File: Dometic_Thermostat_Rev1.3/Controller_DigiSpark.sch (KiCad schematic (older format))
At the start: 22 parts, among them P1 UNREG_12V_IN, P2 UNUSED_MICRO_PINS, P3 RELAY_SW_OUT, P4 RELAY_NC, P5 FUSE_BLOCK, P6 AUX_VOLT_CONN, Q1 2N3904, Q2 2N2222A, T1 Relay_SPDT, U1 7805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

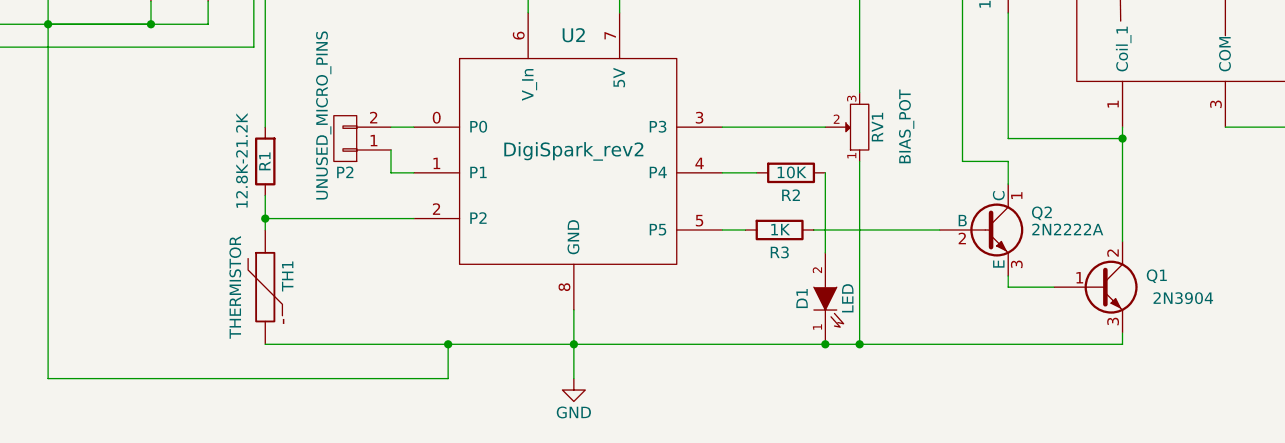
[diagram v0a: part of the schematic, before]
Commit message: Added R4 in || w/ thermistor, value not calculated
Changed thermistor config to series-parallel, increase linearity.
Method detailed at:

http://www.edn.com/design/sensors/4429105/Linearize-thermistors-with-new-formula
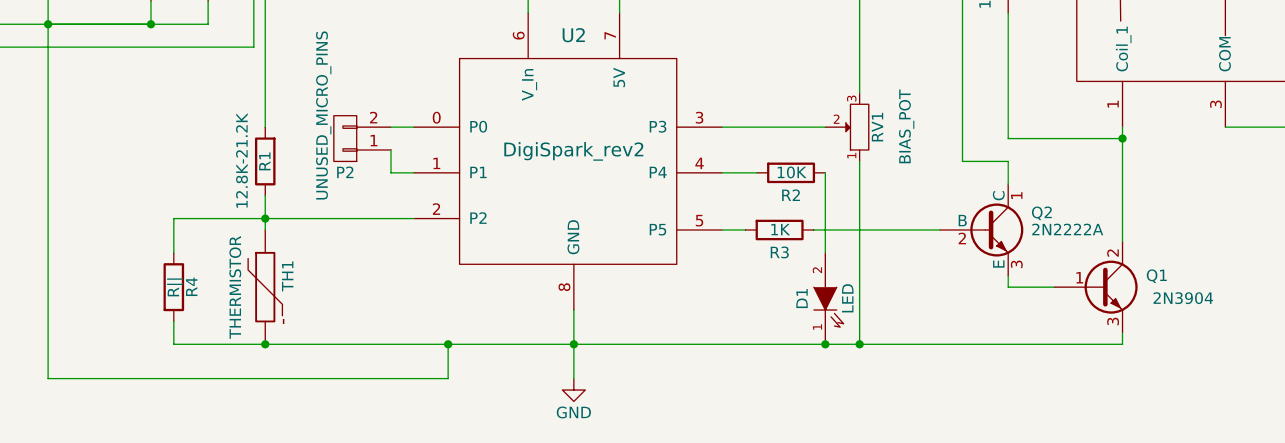
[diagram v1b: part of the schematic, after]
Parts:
- added R4: R||, Resistors_ThroughHole:R_Axial_DIN0309_L9.0mm_D3.2mm_P12.70mm_Horizontal, symbol R
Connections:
- net GND: now also R4.2
- net at R1.1, TH1.1, U2.2 (P2): now also R4.1
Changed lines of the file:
@@
 	2550 3000 2550 3150
 Wire Wire Line
-	3200 3100 2550 3100
+	2150 3100 3200 3100
 Connection ~ 2550 3100
 Wire Wire Line
-	2550 3650 6300 3650
+	2150 3650 6300 3650
 Connection ~ 3900 3650
 Wire Wire Line
@@
 Wire Wire Line
 	6300 3650 6300 3600
+$Comp
+L R R4
+U 1 1 59015000
+P 2150 3400
+F 0 "R4" V 2230 3400 50  0000 C CNN
+F 1 "R||" V 2150 3400 50  0000 C CNN
+F 2 "Resistors_ThroughHole:R_Axial_DIN0309_L9.0mm_D3.2mm_P12.70mm_Horizontal" V 2080 3400 50  0001 C CNN
+F 3 "" H 2150 3400 50  0000 C CNN
+	1    2150 3400
+	1    0    0    -1
+$EndComp
+Wire Wire Line
+	2150 3250 2150 3100
+Wire Wire Line
+	2150 3550 2150 3650
+Connection ~ 2550 3650
 $EndSCHEMATC

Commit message: Add R4, change footprints TH1 & LED
Added R4 to board, changed thermistor and LED footprints.
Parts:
- D1: footprint LEDs:LED_D3.0mm -> LEDs:LED_D5.0mm
- TH1: footprint COMPLIB:SolderWirePad_2x_1-5mmDrill-CUSTOMWIDE -> COMPLIB:Therm_Wire_Mounts
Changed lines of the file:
@@
 F 0 "TH1" V 2650 3450 50  0000 C CNN
 F 1 "THERMISTOR" V 2450 3400 50  0000 C BNN
-F 2 "COMPLIB:SolderWirePad_2x_1-5mmDrill-CUSTOMWIDE" H 2550 3400 50  0001 C CNN
+F 2 "COMPLIB:Therm_Wire_Mounts" H 2550 3400 50  0001 C CNN
 F 3 "" H 2550 3400 50  0000 C CNN
 	1    2550 3400
@@
 F 0 "D1" H 5000 3550 50  0000 C CNN
 F 1 "LED" H 5000 3350 50  0000 C CNN
-F 2 "LEDs:LED_D3.0mm" H 5000 3450 50  0001 C CNN
+F 2 "LEDs:LED_D5.0mm" H 5000 3450 50  0001 C CNN
 F 3 "" H 5000 3450 50  0000 C CNN
 	1    5000 3450

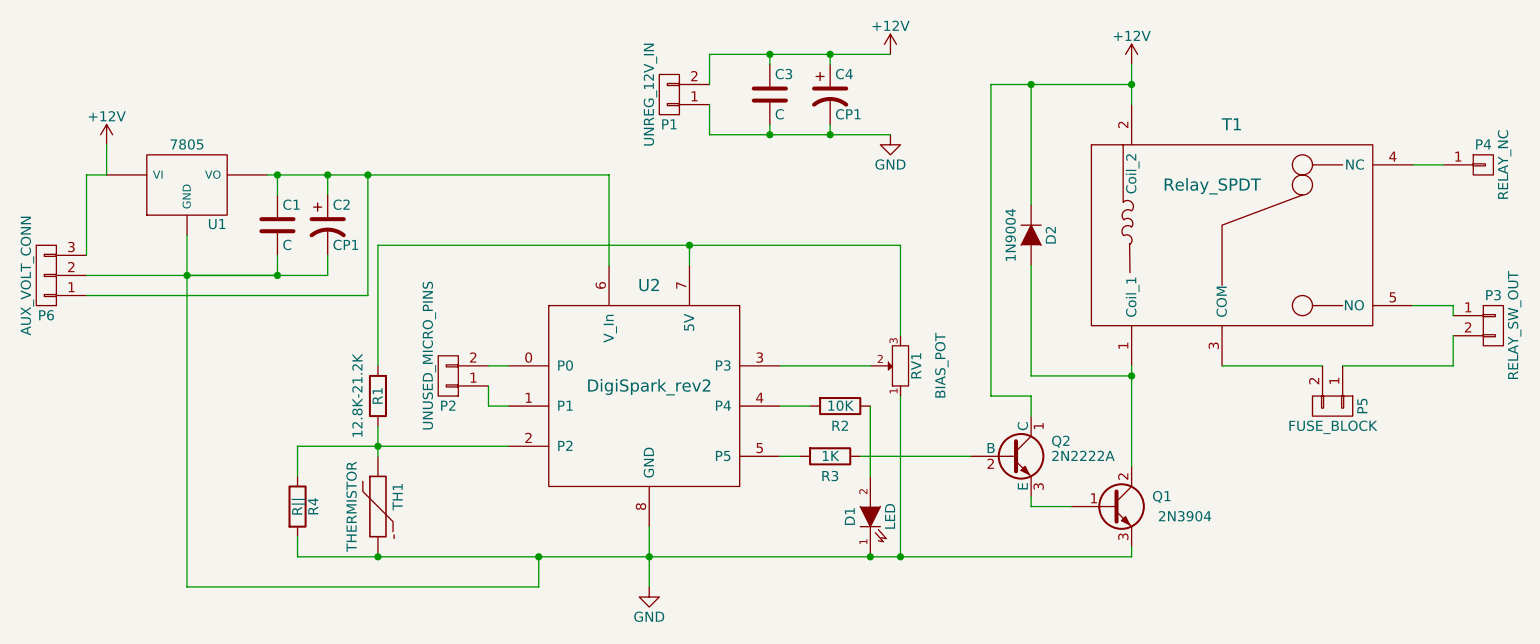
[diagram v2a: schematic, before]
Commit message: Changed Schematic-updated relay driver to mosfet
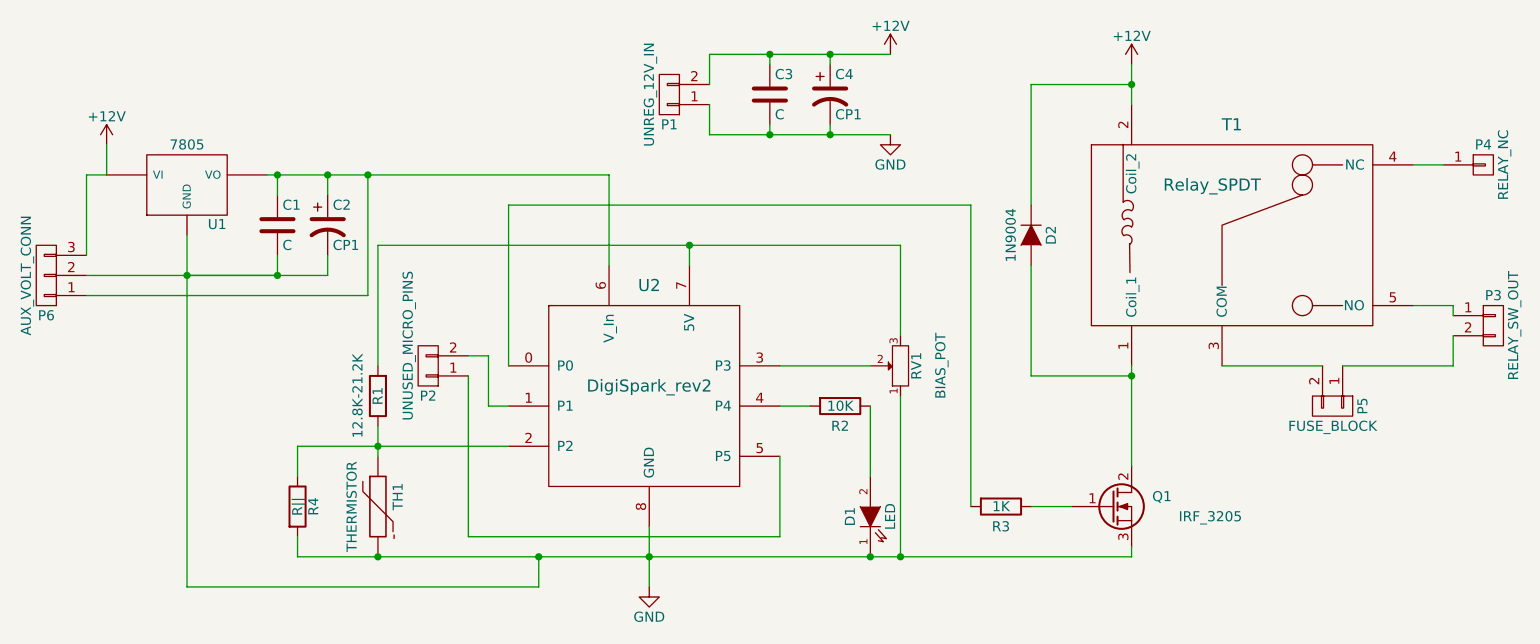
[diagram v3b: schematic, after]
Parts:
- removed Q1: 2N3904, TO_SOT_Packages_THT:TO-220_Horizontal, symbol Q_NPN_BCE
- removed Q2: 2N2222A, TO_SOT_Packages_THT:TO-92_Inline_Wide, symbol BC413
- added Q1: IRF_3205, symbol Q_NMOS_GDS
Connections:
- net GND: now also Q1.3 (S)
- net at U2.0 (P0): now also R3.2; no longer P2.2 (P2)
- net at U2.1 (P1): now also P2.2 (P2); no longer P2.1 (P1)
- net at U2.5 (P5): now also P2.1 (P1); no longer R3.2
- net at R3.1: now also Q1.1 (G)
- net at D2.2 (A), T1.1 (Coil_1): now also Q1.2 (D)
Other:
- moved on the sheet: P2, R3
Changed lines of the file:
@@
 L R R3
 U 1 1 58FFC6C2
-P 4800 3150
-F 0 "R3" V 4900 3150 50  0000 C CNN
-F 1 "1K" V 4800 3150 50  0000 C CNN
-F 2 "Resistors_ThroughHole:R_Axial_DIN0309_L9.0mm_D3.2mm_P12.70mm_Horizontal" V 4730 3150 50  0001 C CNN
-F 3 "" H 4800 3150 50  0000 C CNN
-	1    4800 3150
+P 5650 3400
+F 0 "R3" V 5750 3400 50  0000 C CNN
+F 1 "1K" V 5650 3400 50  0000 C CNN
+F 2 "Resistors_ThroughHole:R_Axial_DIN0309_L9.0mm_D3.2mm_P12.70mm_Horizontal" V 5580 3400 50  0001 C CNN
+F 3 "" H 5650 3400 50  0000 C CNN
+	1    5650 3400
 	0    1    1    0
-$EndComp
-$Comp
-L Q_NPN_BCE Q1
-U 1 1 58FFC83C
-P 6200 3400
-F 0 "Q1" H 6500 3450 50  0000 R CNN
-F 1 "2N3904" H 6700 3350 50  0000 R CNN
-F 2 "TO_SOT_Packages_THT:TO-220_Horizontal" H 6400 3500 50  0001 C CNN
-F 3 "" H 6200 3400 50  0000 C CNN
-	1    6200 3400
-	1    0    0    -1
 $EndComp
 $Comp
@@
 L CONN_01X02 P2
 U 1 1 58FFEBFE
-P 2900 2750
-F 0 "P2" H 2900 2900 50  0000 C CNN
-F 1 "UNUSED_MICRO_PINS" V 3000 2650 50  0000 C CNN
-F 2 "Pin_Headers:Pin_Header_Straight_1x02_Pitch2.00mm" H 2900 2750 50  0001 C CNN
-F 3 "" H 2900 2750 50  0000 C CNN
-	1    2900 2750
+P 2800 2700
+F 0 "P2" H 2800 2850 50  0000 C CNN
+F 1 "UNUSED_MICRO_PINS" V 2900 2600 50  0000 C CNN
+F 2 "Pin_Headers:Pin_Header_Straight_1x02_Pitch2.00mm" H 2800 2700 50  0001 C CNN
+F 3 "" H 2800 2700 50  0000 C CNN
+	1    2800 2700
 	-1   0    0    1
 $EndComp
@@
 	1    0    0    -1
 $EndComp
-Wire Wire Line
-	5000 2700 4550 2700
-Wire Wire Line
-	5150 2100 5150 2550
-Wire Wire Line
-	4550 2900 4700 2900
-Wire Wire Line
-	3900 3500 3900 3800
-Wire Wire Line
-	2550 3000 2550 3150
-Wire Wire Line
-	2150 3100 3200 3100
-Connection ~ 2550 3100
-Wire Wire Line
-	2150 3650 6300 3650
-Connection ~ 3900 3650
-Wire Wire Line
-	2550 2700 2550 2100
-Wire Wire Line
-	2550 2100 5150 2100
-Wire Wire Line
-	4100 2100 4100 2200
-Wire Wire Line
-	2000 1750 3700 1750
-Wire Wire Line
-	3700 1750 3700 2200
-Wire Wire Line
-	1600 3800 3350 3800
-Wire Wire Line
-	3350 3800 3350 3650
-Connection ~ 3350 3650
-Connection ~ 4100 2100
-Wire Wire Line
-	5000 2900 5000 3250
-Wire Wire Line
-	5150 3650 5150 2850
-Connection ~ 5000 3650
-Connection ~ 5150 3650
-Wire Wire Line
-	6300 2700 6300 3200
-Wire Wire Line
-	6300 1200 6300 1400
-Wire Wire Line
-	5800 1900 5800 1300
-Wire Wire Line
-	5600 1300 6300 1300
-Connection ~ 6300 1300
-Wire Wire Line
-	3100 2700 3200 2700
-Wire Wire Line
-	3100 2800 3100 2900
-Wire Wire Line
-	3100 2900 3200 2900
-Wire Wire Line
-	4200 1550 5100 1550
-Wire Wire Line
-	4800 1550 4800 1500
-Wire Wire Line
-	4500 1550 4500 1500
-Connection ~ 4800 1550
-Wire Wire Line
-	4200 1550 4200 1400
-Connection ~ 4500 1550
-Wire Wire Line
-	4200 1300 4200 1150
-Wire Wire Line
-	4200 1150 5100 1150
-Wire Wire Line
-	4500 1150 4500 1200
-Wire Wire Line
-	4800 1150 4800 1200
-Connection ~ 4500 1150
-Connection ~ 4800 1150
-Wire Wire Line
-	2300 1750 2300 1850
-Connection ~ 2300 1750
-Wire Wire Line
-	2050 1750 2050 1850
-Connection ~ 2050 1750
-Wire Wire Line
-	1200 1600 1200 1750
 $Comp
 L Relay_SPDT T1
@@
 	1    0    0    -1
 $EndComp
-Wire Wire Line
-	7700 2400 7900 2400
-Wire Wire Line
-	7900 2400 7900 2450
-Wire Wire Line
-	7900 2700 7900 2550
-Wire Wire Line
-	7700 1700 7850 1700
 $Comp
 L CONN_01X02 P5
@@
 	0    1    1    0
 $EndComp
-Wire Wire Line
-	6750 2700 7250 2700
-Wire Wire Line
-	7350 2700 7900 2700
 $Comp
 L CONN_01X03 P6
@@
 	-1   0    0    1
 $EndComp
-Wire Wire Line
-	1100 2150 1100 1750
-Wire Wire Line
-	1100 1750 1200 1750
-Wire Wire Line
-	1100 2350 2500 2350
-Wire Wire Line
-	2500 2350 2500 1750
-Connection ~ 2500 1750
-Wire Wire Line
-	1600 2050 1600 3800
-Wire Wire Line
-	2050 2150 2050 2250
-Wire Wire Line
-	2050 2250 1100 2250
-Wire Wire Line
-	1600 2250 2300 2250
-Wire Wire Line
-	2300 2250 2300 2150
-Connection ~ 1600 2250
-Connection ~ 2050 2250
-$Comp
-L BC413 Q2
-U 1 1 59000F61
-P 5700 3150
-F 0 "Q2" H 5900 3225 50  0000 L CNN
-F 1 "2N2222A" H 5900 3150 50  0000 L CNN
-F 2 "TO_SOT_Packages_THT:TO-92_Inline_Wide" H 5900 3075 50  0001 L CIN
-F 3 "" H 5700 3150 50  0000 L CNN
-	1    5700 3150
-	1    0    0    -1
-$EndComp
-Wire Wire Line
-	4550 3150 4650 3150
-Wire Wire Line
-	4950 3150 5500 3150
-Wire Wire Line
-	5800 2200 5800 2750
-Wire Wire Line
-	5800 2750 6300 2750
-Connection ~ 6300 2750
-Wire Wire Line
-	5800 2950 5800 2850
-Wire Wire Line
-	5800 2850 5600 2850
-Wire Wire Line
-	5600 2850 5600 1300
-Connection ~ 5800 1300
-Wire Wire Line
-	5800 3350 5800 3400
-Wire Wire Line
-	5800 3400 6000 3400
-Wire Wire Line
-	6300 3650 6300 3600
 $Comp
 L R R4
@@
 	1    0    0    -1
 $EndComp
+$Comp
+L Q_NMOS_GDS Q1
+U 1 1 5918BB56
+P 6200 3400
+F 0 "Q1" H 6500 3450 50  0000 R CNN
+F 1 "IRF_3205" H 6850 3350 50  0000 R CNN
+F 2 "" H 6400 3500 50  0000 C CNN
+F 3 "" H 6200 3400 50  0000 C CNN
+	1    6200 3400
+	1    0    0    -1
+$EndComp
+Wire Wire Line
+	5000 2700 4550 2700
+Wire Wire Line
+	5150 2100 5150 2550
+Wire Wire Line
+	4550 2900 4700 2900
+Wire Wire Line
+	3900 3500 3900 3800
+Wire Wire Line
+	2550 3000 2550 3150
+Wire Wire Line
+	2150 3100 3200 3100
+Connection ~ 2550 3100
+Wire Wire Line
+	2150 3650 6300 3650
+Connection ~ 3900 3650
+Wire Wire Line
+	2550 2700 2550 2100
+Wire Wire Line
+	2550 2100 5150 2100
+Wire Wire Line
+	4100 2100 4100 2200
+Wire Wire Line
+	2000 1750 3700 1750
+Wire Wire Line
+	3700 1750 3700 2200
+Wire Wire Line
+	1600 3800 3350 3800
+Wire Wire Line
+	3350 3800 3350 3650
+Connection ~ 3350 3650
+Connection ~ 4100 2100
+Wire Wire Line
+	5000 2900 5000 3250
+Wire Wire Line
+	5150 3650 5150 2850
+Connection ~ 5000 3650
+Connection ~ 5150 3650
+Wire Wire Line
+	6300 2700 6300 3200
+Wire Wire Line
+	6300 1200 6300 1400
+Wire Wire Line
+	4200 1550 5100 1550
+Wire Wire Line
+	4800 1550 4800 1500
+Wire Wire Line
+	4500 1550 4500 1500
+Connection ~ 4800 1550
+Wire Wire Line
+	4200 1550 4200 1400
+Connection ~ 4500 1550
+Wire Wire Line
+	4200 1300 4200 1150
+Wire Wire Line
+	4200 1150 5100 1150
+Wire Wire Line
+	4500 1150 4500 1200
+Wire Wire Line
+	4800 1150 4800 1200
+Connection ~ 4500 1150
+Connection ~ 4800 1150
+Wire Wire Line
+	2300 1750 2300 1850
+Connection ~ 2300 1750
+Wire Wire Line
+	2050 1750 2050 1850
+Connection ~ 2050 1750
+Wire Wire Line
+	1200 1600 1200 1750
+Wire Wire Line
+	7700 2400 7900 2400
+Wire Wire Line
+	7900 2400 7900 2450
+Wire Wire Line
+	7900 2700 7900 2550
+Wire Wire Line
+	7700 1700 7850 1700
+Wire Wire Line
+	6750 2700 7250 2700
+Wire Wire Line
+	7350 2700 7900 2700
+Wire Wire Line
+	1100 2150 1100 1750
+Wire Wire Line
+	1100 1750 1200 1750
+Wire Wire Line
+	1100 2350 2500 2350
+Wire Wire Line
+	2500 2350 2500 1750
+Connection ~ 2500 1750
+Wire Wire Line
+	1600 2050 1600 3800
+Wire Wire Line
+	2050 2150 2050 2250
+Wire Wire Line
+	2050 2250 1100 2250
+Wire Wire Line
+	1600 2250 2300 2250
+Wire Wire Line
+	2300 2250 2300 2150
+Connection ~ 1600 2250
+Connection ~ 2050 2250
+Wire Wire Line
+	5800 2200 5800 2750
+Wire Wire Line
+	5800 2750 6300 2750
+Connection ~ 6300 2750
+Wire Wire Line
+	6300 3650 6300 3600
 Wire Wire Line
 	2150 3250 2150 3100
@@
 	2150 3550 2150 3650
 Connection ~ 2550 3650
+Wire Wire Line
+	6300 1300 5800 1300
+Wire Wire Line
+	5800 1300 5800 1900
+Connection ~ 6300 1300
+Wire Wire Line
+	3200 2700 3200 1900
+Wire Wire Line
+	3200 1900 5500 1900
+Wire Wire Line
+	5500 1900 5500 3400
+Wire Wire Line
+	5800 3400 6000 3400
+Wire Wire Line
+	3000 2650 3100 2650
+Wire Wire Line
+	3100 2650 3100 2900
+Wire Wire Line
+	3100 2900 3200 2900
+Wire Wire Line
+	3000 2750 3000 3550
+Wire Wire Line
+	3000 3550 4550 3550
+Wire Wire Line
+	4550 3550 4550 3150
 $EndSCHEMATC

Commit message: Schematic- changed pin assignment, changed darlington to mosfet
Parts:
- Q1: footprint (none) -> TO_SOT_Packages_THT:TO-220_Horizontal
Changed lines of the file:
@@
 F 0 "Q1" H 6500 3450 50  0000 R CNN
 F 1 "IRF_3205" H 6850 3350 50  0000 R CNN
-F 2 "" H 6400 3500 50  0000 C CNN
+F 2 "TO_SOT_Packages_THT:TO-220_Horizontal" H 6400 3500 50  0001 C CNN
 F 3 "" H 6200 3400 50  0000 C CNN
 	1    6200 3400

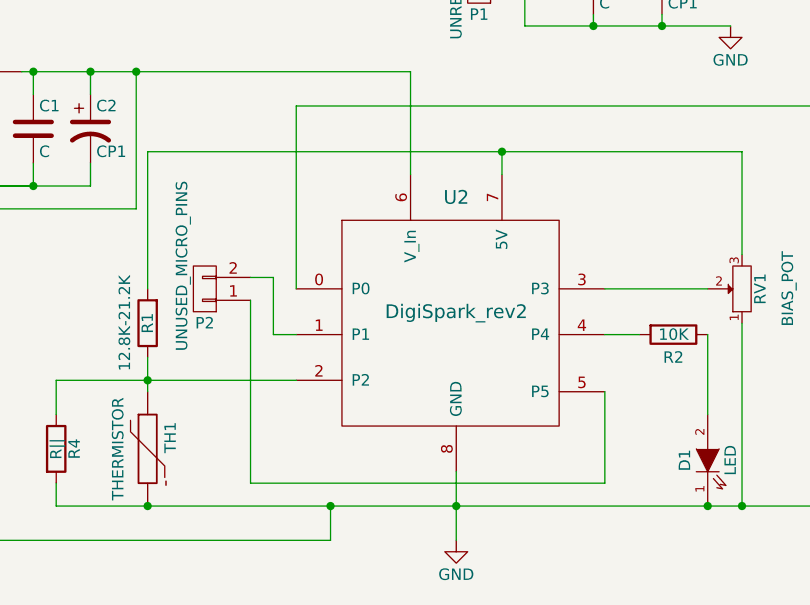
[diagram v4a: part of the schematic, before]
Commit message: Changed PCB-updated pin assg & added mount holes
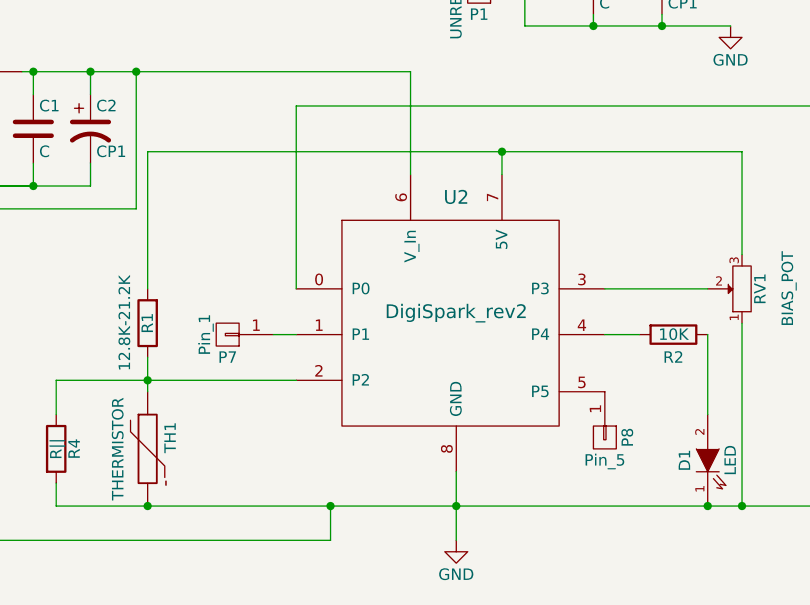
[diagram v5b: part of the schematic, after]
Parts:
- removed P2: UNUSED_MICRO_PINS, Pin_Headers:Pin_Header_Straight_1x02_Pitch2.00mm, symbol CONN_01X02
- added P7: Pin_1, Wire_Pads:SolderWirePad_single_0-8mmDrill, symbol CONN_01X01
- added P8: Pin_5, Wire_Pads:SolderWirePad_single_0-8mmDrill, symbol CONN_01X01
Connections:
- net at U2.1 (P1): now also P7.1 (P1)
- net at U2.5 (P5): now also P8.1 (P1)
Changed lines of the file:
@@
-$EndComp
-$Comp
-L CONN_01X02 P2
-U 1 1 58FFEBFE
-P 2800 2700
-F 0 "P2" H 2800 2850 50  0000 C CNN
-F 1 "UNUSED_MICRO_PINS" V 2900 2600 50  0000 C CNN
-F 2 "Pin_Headers:Pin_Header_Straight_1x02_Pitch2.00mm" H 2800 2700 50  0001 C CNN
-F 3 "" H 2800 2700 50  0000 C CNN
-	1    2800 2700
-	-1   0    0    1
 $EndComp
 $Comp
@@
 	5800 3400 6000 3400
 Wire Wire Line
-	3000 2650 3100 2650
-Wire Wire Line
-	3100 2650 3100 2900
-Wire Wire Line
 	3100 2900 3200 2900
-Wire Wire Line
-	3000 2750 3000 3550
-Wire Wire Line
-	3000 3550 4550 3550
-Wire Wire Line
-	4550 3550 4550 3150
+$Comp
+L CONN_01X01 P7
+U 1 1 5918E43D
+P 2900 2900
+F 0 "P7" H 2900 3000 50  0000 C CNN
+F 1 "Pin_1" V 3000 2900 50  0000 C CNN
+F 2 "Wire_Pads:SolderWirePad_single_0-8mmDrill" H 2900 2900 50  0001 C CNN
+F 3 "" H 2900 2900 50  0000 C CNN
+	1    2900 2900
+	-1   0    0    1
+$EndComp
+$Comp
+L CONN_01X01 P8
+U 1 1 5918EB66
+P 4550 3350
+F 0 "P8" H 4550 3450 50  0000 C CNN
+F 1 "Pin_5" V 4650 3350 50  0000 C CNN
+F 2 "Wire_Pads:SolderWirePad_single_0-8mmDrill" H 4550 3350 50  0001 C CNN
+F 3 "" H 4550 3350 50  0000 C CNN
+	1    4550 3350
+	0    1    1    0
+$EndComp
 $EndSCHEMATC
